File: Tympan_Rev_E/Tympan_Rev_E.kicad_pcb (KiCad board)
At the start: 4 copper layers, 38 x 74 mm, 93 parts, among them IC1 BC127, J1 SJ-3523-SMT-TR, J2 SJ-3524-SMT-TR-PI, J3 Conn_01x06, J4 Qwiik Connector, J5 SMT, J6 SMT, P1 CONN_01X06, P2 CONN_01X06, P3 CONN_01X06, P4 CONN_01X06, P6 CONN_01X01, P7 CONN_01X01, P8 CONN_01X01, SW1 CL-SB-22A, SW2 SW_Push, U1 MCP73831, U2 TLV320AIC3206IRSBT, U3 74LVC1G66, U4 LP5907MFX-1.8, U5 Teensy4.1, U6 LC709203

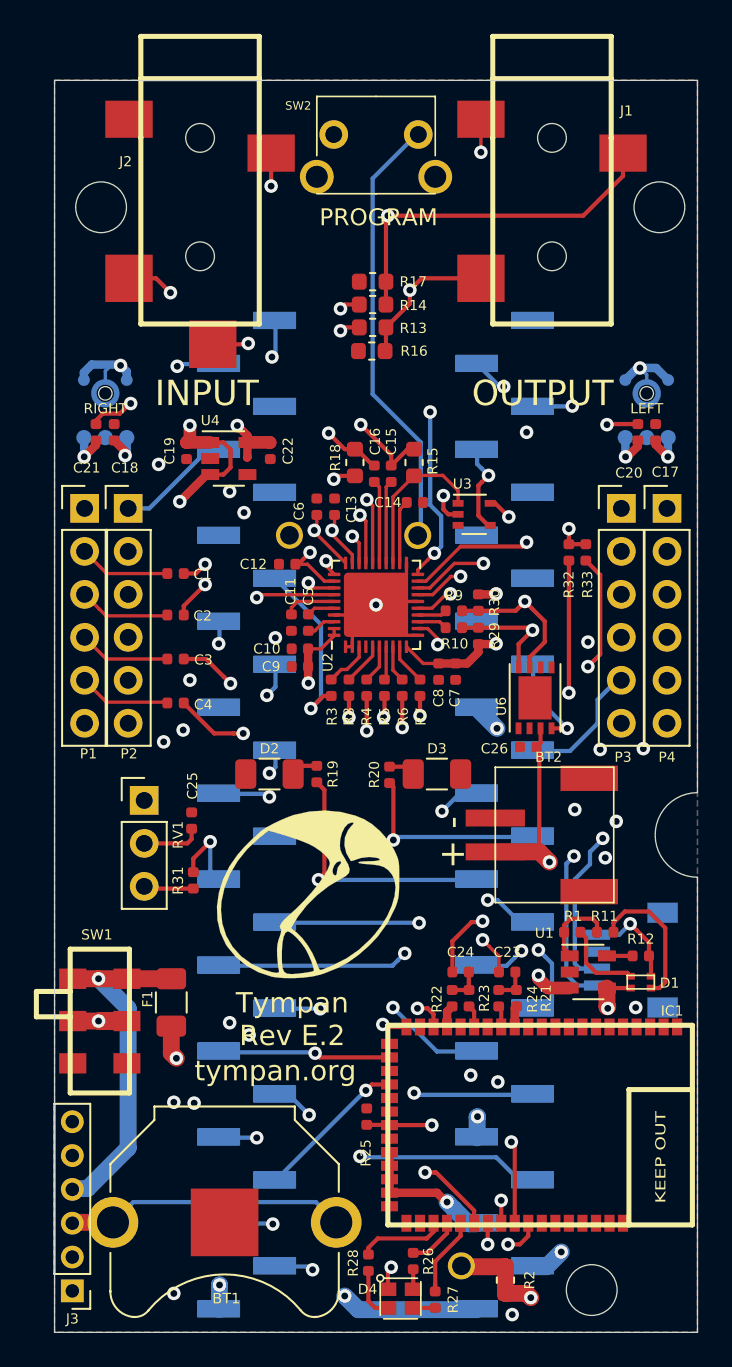
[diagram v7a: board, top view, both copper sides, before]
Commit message: updates to the enclosure files
I'm adding the mods that I made to the enclosure
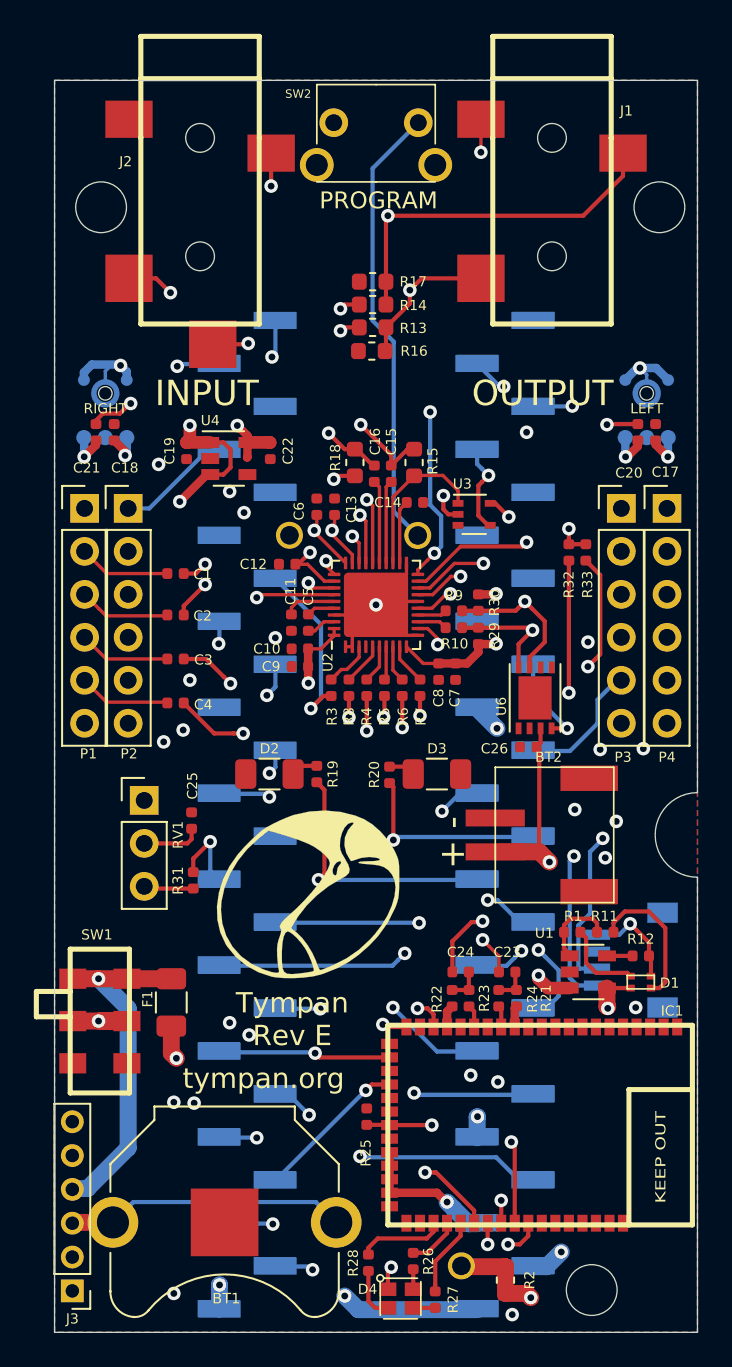
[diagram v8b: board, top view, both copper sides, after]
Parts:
- J5, J6: value SMT -> Conn_01x24
- moved SW2 0.70 mm to (153.4, 61.7)
- moved J6 0.05 mm to (161.1, 102.6)
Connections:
- J4 pad : +3V3 -> (no net)
- J5 pad 1: GND -> Net-(J5-Pad1)
- J5 pad 10: /DOUT -> Net-(J5-Pad10)
- J5 pad 11: /BT_nRESET -> Net-(J5-Pad11)
- J5 pad 12: /SS -> Net-(J5-Pad12)
- J5 pad 13: /MOSI -> Net-(J5-Pad13)
- J5 pad 14: /MISO -> Net-(J5-Pad14)
- J5 pad 16: /SCL2 -> Net-(J5-Pad16)
- J5 pad 17: /SDA2 -> Net-(J5-Pad17)
- J5 pad 18: /nRESET -> Net-(J5-Pad18)
- J5 pad 2: /BT_TX -> Net-(J5-Pad2)
- J5 pad 21: /M_BIAS_1 -> Net-(J5-Pad21)
- J5 pad 23: /nRESET_1 -> Net-(J5-Pad23)
- J5 pad 24: /DIN_1 -> Net-(J5-Pad24)
- J5 pad 3: /BT_RX -> Net-(J5-Pad3)
- J5 pad 4: /BT_PIO5 -> Net-(J5-Pad4)
- J5 pad 5: /BT_CTS -> Net-(J5-Pad5)
- J5 pad 6: /BT_RTS -> Net-(J5-Pad6)
- J5 pad 7: /BT_PIO0 -> Net-(J5-Pad7)
- J5 pad 8: /DOUT_1 -> Net-(J5-Pad8)
- J5 pad 9: /DIN -> Net-(J5-Pad9)
- J6 pad 10: GND -> Net-(J6-Pad10)
- J6 pad 11: /SCK -> Net-(J6-Pad11)
- J6 pad 12: /VREGEN -> Net-(J6-Pad12)
- J6 pad 13: /LED_A -> Net-(J6-Pad13)
- J6 pad 14: /LED_R -> Net-(J6-Pad14)
- J6 pad 15: /POT -> Net-(J6-Pad15)
- J6 pad 16: /SDA -> Net-(J6-Pad16)
- J6 pad 17: /SCL -> Net-(J6-Pad17)
- J6 pad 18: /WCLK -> Net-(J6-Pad18)
- J6 pad 19: /BCLK -> Net-(J6-Pad19)
- J6 pad 2: /34_RX8 -> Net-(J6-Pad2)
- J6 pad 20: GND -> Net-(J6-Pad20)
- J6 pad 21: /MCLK -> Net-(J6-Pad21)
- J6 pad 23: GND -> Net-(J6-Pad23)
- J6 pad 24: /VIN -> Net-(J6-Pad24)
- J6 pad 3: /35_TX8 -> Net-(J6-Pad3)
- J6 pad 4: /M_BIAS -> Net-(J6-Pad4)
- J6 pad 9: /ALARMB -> Net-(J6-Pad9)
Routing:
- net /V_BAT: track 60.3 -> 57.9 mm
- net /HPR: track 24.1 -> 23.5 mm
- net /35_TX8: track 79.7 -> 80.2 mm
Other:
- board text added: "Tympan Rev E"
- board text removed: "Qwiic ———> Stemma"
- board text removed: "Tympan Rev E.2"
